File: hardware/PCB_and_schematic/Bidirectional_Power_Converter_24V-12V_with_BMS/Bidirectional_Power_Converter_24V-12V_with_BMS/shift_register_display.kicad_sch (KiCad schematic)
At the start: 2 parts, among them J6 Conn_02x09_Odd_Even, U4 74HC595

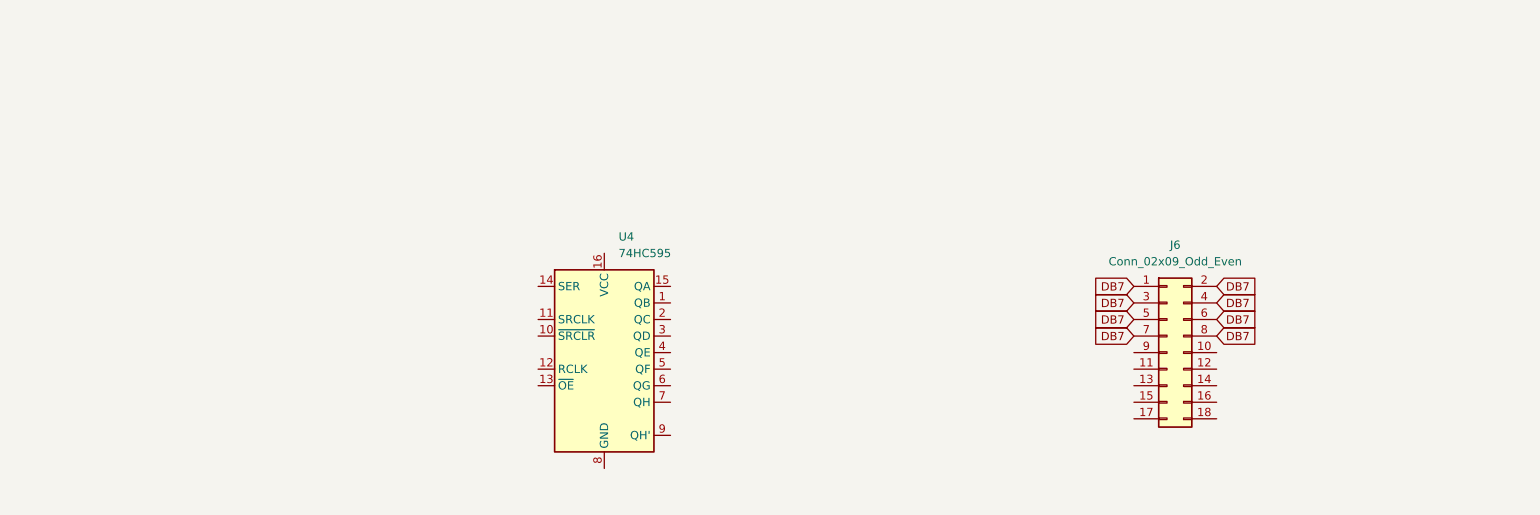
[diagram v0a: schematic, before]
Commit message: Add lcd display spi schematic, update tl494 boost converter
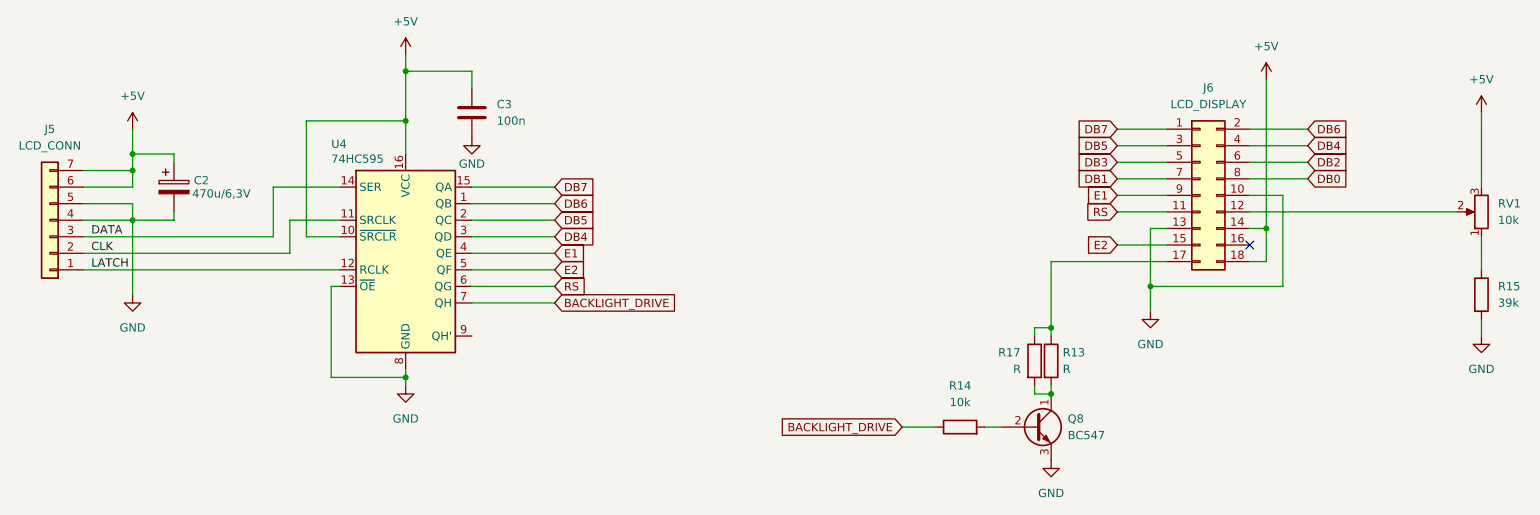
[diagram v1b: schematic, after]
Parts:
- added C2: 470u/6,3V, symbol Device:C_Polarized
- added C3: 100n, symbol Device:C
- added J5: LCD_CONN, symbol Connector_Generic:Conn_01x07
- added Q8: BC547, Package_TO_SOT_THT:TO-92_Inline, symbol Transistor_BJT:BC547
- added R13, R17: R, Resistor_SMD:R_0805_2012Metric, symbol Device:R
- added R14: 10k, Resistor_SMD:R_0805_2012Metric, symbol Device:R
- added R15: 39k, Resistor_SMD:R_0805_2012Metric, symbol Device:R
- added RV1: 10k, Resistor_SMD:R_0805_2012Metric, symbol Device:R_Potentiometer
- J6: value Conn_02x09_Odd_Even -> LCD_DISPLAY
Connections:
- net DB7: now also U4.15 (QA); no longer J6.2 (Pin_2), J6.3 (Pin_3), J6.4 (Pin_4), J6.5 (Pin_5), J6.6 (Pin_6), J6.7 (Pin_7), J6.8 (Pin_8)
- net DB6: now reaches U4.1 (QB)
- net DB6: now also J6.2 (Pin_2)
- net +5V: now reaches U4.10 (~{SRCLR})
- net +5V: now also J6.14 (Pin_14), J6.18 (Pin_18), U4.16 (VCC), C2.1, C3.1, J5.6 (Pin_6), J5.7 (Pin_7), RV1.3
- net CLK: now reaches U4.11 (SRCLK)
- net CLK: now also J5.2 (Pin_2)
- net LATCH: now reaches U4.12 (RCLK)
- net LATCH: now also J5.1 (Pin_1)
- net GND: now reaches U4.13 (~{OE})
- net GND: now also J6.10 (Pin_10), J6.13 (Pin_13), U4.8 (GND), C2.2, C3.2, J5.4 (Pin_4), J5.5 (Pin_5), Q8.3 (E), R15.2
- net DATA: now reaches U4.14 (SER)
- net DATA: now also J5.3 (Pin_3)
- net DB5: now reaches U4.2 (QC)
- net DB5: now also J6.3 (Pin_3)
- net DB4: now reaches U4.3 (QD)
- net DB4: now also J6.4 (Pin_4)
- net E1: now reaches U4.4 (QE)
- net E1: now also J6.9 (Pin_9)
- net E2: now reaches U4.5 (QF)
- net E2: now also J6.15 (Pin_15)
- net RS: now reaches U4.6 (QG)
- net RS: now also J6.11 (Pin_11)
- net BACKLIGHT_DRIVE: now reaches U4.7 (QH)
- net BACKLIGHT_DRIVE: now also R14.1
- net at J6.12 (Pin_12): now also RV1.2
- net at J6.17 (Pin_17): now also R13.1, R17.1
- new net: R15.1, RV1.1
- new net: Q8.1 (C), R13.2, R17.2
- new net: Q8.2 (B), R14.2
- new net DB0: J6.8 (Pin_8)
- new net DB1: J6.7 (Pin_7)
- new net DB2: J6.6 (Pin_6)
- new net DB3: J6.5 (Pin_5)
- no-connect marks 0 -> 1
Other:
- moved on the sheet: J6, U4
